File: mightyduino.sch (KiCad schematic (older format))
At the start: 20 parts, among them IC1 ATMEGA644P-A, P1 CONN_01X18, P2 CONN_01X06, P3 CONN_01X18, SW1 RESET, U1 MIC5219-3.3YM5, X1 CSTCE 16MHZ

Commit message: switched led from d13 to d0, cosmetic improvments
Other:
- note added: "<16v"
- note added: "RAW -> input voltage before the voltage regulator \nVCC -> output voltage of the regulator, IC voltage"
- note added: "U1\n MIC5219-xxYM5 -> xx = voltage 1.8->5v\n \nX1\n CSTCE 16MOV53-R0 4-20Mhz"
- note removed: "4-16v"
- note removed: "U1\n MIC5219-3.3YM5 -> 3.3v core\n MIC5219-5.0YM5 -> 5v core\n\nX1\n CSTCE 16MOV53-R0 4-20Mhz"
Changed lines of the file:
@@
 Sheet 1 1
 Title "Mightyduino"
-Date "2016-11-21"
-Rev "1.0"
+Date "2016-12-7"
+Rev "1.1"
 Comp "dev76.org"
 Comment1 "Mightyduino is an arduino based on Atmega 644p/1024p "
@@
 $EndComp
 Text Label 4400 6400 0    59   Italic 0
-D13
+D0
 $Comp
 L CONN_01X06 P2
@@
 RAW
 Text Notes 8900 2000 0    43   ~ 0
-4-16v
+<16v
 $Comp
 L GND #PWR018
@@
 Wire Wire Line
 	2850 7200 2850 7150
-Text Notes 4700 6100 0    60   ~ 0
-U1\n  MIC5219-3.3YM5  -> 3.3v core\n  MIC5219-5.0YM5  -> 5v core\n\nX1\n  CSTCE 16MOV53-R0  4-20Mhz
+Text Notes 8750 6300 0    60   ~ 0
+U1\n  MIC5219-xxYM5  -> xx = voltage 1.8->5v\n  \nX1\n  CSTCE 16MOV53-R0  4-20Mhz
 Wire Wire Line
 	1400 6600 1950 6600
+Text Notes 700  6250 0    60   ~ 0
+RAW -> input voltage before the voltage regulator \nVCC -> output voltage of the regulator, IC voltage
 $EndSCHEMATC

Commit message: updated ressonator 3d design
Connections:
- wire segments 125 -> 126
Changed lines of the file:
@@
 Sheet 1 1
 Title "Mightyduino"
-Date "2016-12-7"
-Rev "1.1"
+Date "2016-12-9"
+Rev "1.2"
 Comp "dev76.org"
 Comment1 "Mightyduino is an arduino based on Atmega 644p/1024p "
@@
 	1    0    0    -1
 $EndComp
-$Comp
-L GND #PWR011
-U 1 1 5841BFB1
-P 1950 6850
-F 0 "#PWR011" H 1950 6600 50  0001 C CNN
-F 1 "GND" H 1950 6700 50  0000 C CNN
-F 2 "" H 1950 6850 50  0000 C CNN
-F 3 "" H 1950 6850 50  0000 C CNN
-	1    1950 6850
-	1    0    0    -1
-$EndComp
 Text Label 900  6600 2    60   ~ 0
 RAW
@@
 $EndComp
 $Comp
-L GND #PWR012
+L GND #PWR011
 U 1 1 5841CAAD
 P 3750 7500
-F 0 "#PWR012" H 3750 7250 50  0001 C CNN
+F 0 "#PWR011" H 3750 7250 50  0001 C CNN
 F 1 "GND" H 3750 7350 50  0000 C CNN
 F 2 "" H 3750 7500 50  0000 C CNN
@@
 $EndComp
 $Comp
-L VCC #PWR013
+L VCC #PWR012
 U 1 1 583847ED
 P 5350 6750
-F 0 "#PWR013" H 5350 6600 50  0001 C CNN
+F 0 "#PWR012" H 5350 6600 50  0001 C CNN
 F 1 "VCC" H 5350 6900 50  0000 C CNN
 F 2 "" H 5350 6750 50  0000 C CNN
@@
 $EndComp
 $Comp
-L GND #PWR014
+L GND #PWR013
 U 1 1 5841EC2B
 P 1400 1200
-F 0 "#PWR014" H 1400 950 50  0001 C CNN
+F 0 "#PWR013" H 1400 950 50  0001 C CNN
 F 1 "GND" H 1400 1050 50  0000 C CNN
 F 2 "" H 1400 1200 50  0000 C CNN
@@
 RAW
 $Comp
-L GND #PWR015
+L GND #PWR014
 U 1 1 584206C2
 P 7750 4700
-F 0 "#PWR015" H 7750 4450 50  0001 C CNN
+F 0 "#PWR014" H 7750 4450 50  0001 C CNN
 F 1 "GND" H 7750 4550 50  0000 C CNN
 F 2 "" H 7750 4700 50  0000 C CNN
@@
 $EndComp
 $Comp
-L GND #PWR016
+L GND #PWR015
 U 1 1 58420BD7
 P 9300 4650
-F 0 "#PWR016" H 9300 4400 50  0001 C CNN
+F 0 "#PWR015" H 9300 4400 50  0001 C CNN
 F 1 "GND" H 9300 4500 50  0000 C CNN
 F 2 "" H 9300 4650 50  0000 C CNN
@@
 $EndComp
 $Comp
-L GND #PWR017
+L GND #PWR016
 U 1 1 5842144D
 P 4850 7350
-F 0 "#PWR017" H 4850 7100 50  0001 C CNN
+F 0 "#PWR016" H 4850 7100 50  0001 C CNN
 F 1 "GND" H 4850 7200 50  0000 C CNN
 F 2 "" H 4850 7350 50  0000 C CNN
@@
 <16v
 $Comp
-L GND #PWR018
+L GND #PWR017
 U 1 1 58422776
 P 9350 1900
-F 0 "#PWR018" H 9350 1650 50  0001 C CNN
+F 0 "#PWR017" H 9350 1650 50  0001 C CNN
 F 1 "GND" H 9350 1750 50  0000 C CNN
 F 2 "" H 9350 1900 50  0000 C CNN
@@
 $EndComp
 $Comp
-L VCC #PWR019
+L VCC #PWR018
 U 1 1 58420A99
 P 7250 4250
-F 0 "#PWR019" H 7250 4100 50  0001 C CNN
+F 0 "#PWR018" H 7250 4100 50  0001 C CNN
 F 1 "VCC" H 7250 4400 50  0000 C CNN
 F 2 "" H 7250 4250 50  0000 C CNN
@@
 $EndComp
 $Comp
-L VCC #PWR020
+L VCC #PWR019
 U 1 1 5841E709
 P 3350 6400
-F 0 "#PWR020" H 3350 6250 50  0001 C CNN
+F 0 "#PWR019" H 3350 6250 50  0001 C CNN
 F 1 "VCC" H 3350 6550 50  0000 C CNN
 F 2 "" H 3350 6400 50  0000 C CNN
@@
 $EndComp
 $Comp
-L VCC #PWR021
+L VCC #PWR020
 U 1 1 58384873
 P 3750 1050
-F 0 "#PWR021" H 3750 900 50  0001 C CNN
+F 0 "#PWR020" H 3750 900 50  0001 C CNN
 F 1 "VCC" H 3750 1200 50  0000 C CNN
 F 2 "" H 3750 1050 50  0000 C CNN
@@
 $EndComp
 $Comp
-L VCC #PWR022
+L VCC #PWR021
 U 1 1 584228A1
 P 8800 1600
-F 0 "#PWR022" H 8800 1450 50  0001 C CNN
+F 0 "#PWR021" H 8800 1450 50  0001 C CNN
 F 1 "VCC" H 8800 1750 50  0000 C CNN
 F 2 "" H 8800 1600 50  0000 C CNN
@@
 Wire Wire Line
 	3750 6600 3750 6800
-Wire Wire Line
-	1950 6850 1950 6750
 Wire Wire Line
 	8700 3650 9100 3650
@@
 	2850 6750 2850 6950
 $Comp
-L GND #PWR023
+L GND #PWR022
 U 1 1 58435E1F
 P 2850 7200
-F 0 "#PWR023" H 2850 6950 50  0001 C CNN
+F 0 "#PWR022" H 2850 6950 50  0001 C CNN
 F 1 "GND" H 2850 7050 50  0000 C CNN
 F 2 "" H 2850 7200 50  0000 C CNN
@@
 Text Notes 700  6250 0    60   ~ 0
 RAW -> input voltage before the voltage regulator \nVCC -> output voltage of the regulator, IC voltage
+Wire Wire Line
+	1950 6750 1900 6750
+Wire Wire Line
+	1900 6750 1900 6600
+Connection ~ 1900 6600
 $EndSCHEMATC

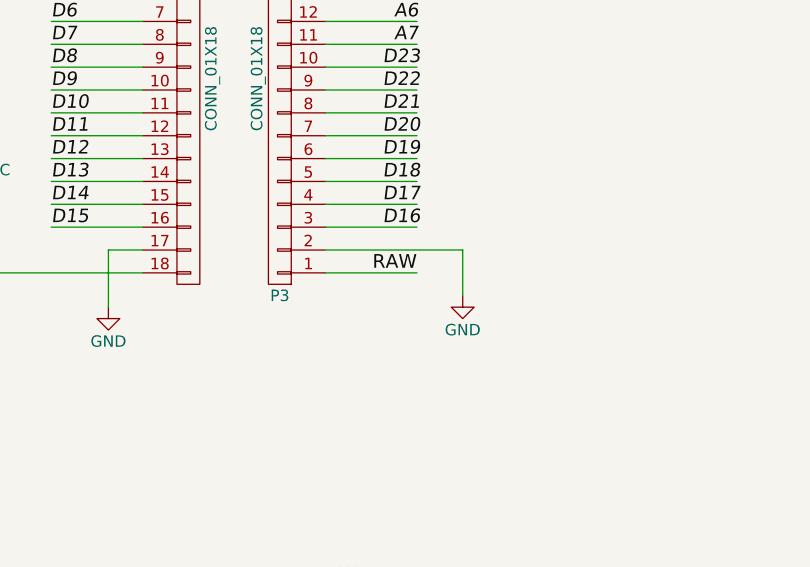
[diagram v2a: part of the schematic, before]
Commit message: C1,C3 better footprint, added RESET PIN
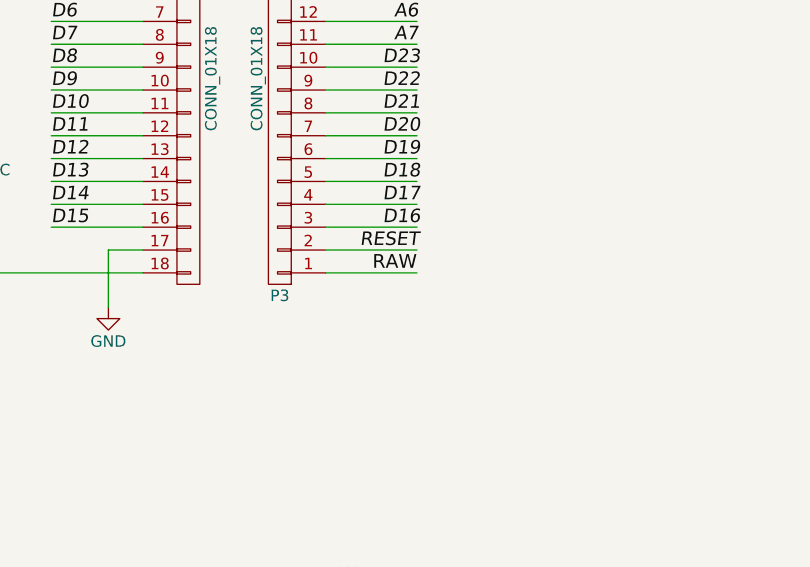
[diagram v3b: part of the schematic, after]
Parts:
- C1, C3: footprint Capacitors_SMD:C_0805 -> Capacitors_Tantalum_SMD:TantalC_SizeA_EIA-3216_Reflow
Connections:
- wire segments 126 -> 125
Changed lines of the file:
@@
 EESchema Schematic File Version 2
+LIBS:mightyduino-rescue
 LIBS:power
 LIBS:device
@@
 Sheet 1 1
 Title "Mightyduino"
-Date "2016-12-9"
-Rev "1.2"
+Date "2017-01-7"
+Rev "1.3"
 Comp "dev76.org"
 Comment1 "Mightyduino is an arduino based on Atmega 644p/1024p "
@@
 $EndComp
 $Comp
-L GND #PWR01
+L GND-RESCUE-mightyduino #PWR01
 U 1 1 58332308
 P 2050 2400
@@
 Murata\nResonator
 $Comp
-L GND #PWR02
+L GND-RESCUE-mightyduino #PWR02
 U 1 1 5833230F
 P 3500 5850
@@
 $EndComp
 $Comp
-L GND #PWR03
+L GND-RESCUE-mightyduino #PWR03
 U 1 1 58332331
 P 2300 3500
@@
 $EndComp
 $Comp
-L GND #PWR04
+L GND-RESCUE-mightyduino #PWR04
 U 1 1 583323B4
 P 5350 7350
@@
 $EndComp
 $Comp
-L GND #PWR06
+L GND-RESCUE-mightyduino #PWR06
 U 1 1 583323CB
 P 5900 7400
@@
 A7
 $Comp
-L GND #PWR07
+L GND-RESCUE-mightyduino #PWR07
 U 1 1 5834C09B
 P 2400 7000
@@
 $EndComp
 $Comp
-L GND #PWR08
+L GND-RESCUE-mightyduino #PWR08
 U 1 1 5834C1DF
 P 3150 7100
@@
 F 0 "C3" H 3360 6920 50  0000 L CNN
 F 1 "10u" H 3360 6770 50  0000 L CNN
-F 2 "Capacitors_SMD:C_0805" H 3350 6850 50  0001 C CNN
+F 2 "Capacitors_Tantalum_SMD:TantalC_SizeA_EIA-3216_Reflow" H 3350 6850 50  0001 C CNN
 F 3 "" H 3350 6850 50  0000 C CNN
 	1    3350 6850
@@
 $EndComp
 $Comp
-L GND #PWR09
+L GND-RESCUE-mightyduino #PWR09
 U 1 1 5838459A
 P 3350 7100
@@
 F 0 "C1" H 1810 6920 50  0000 L CNN
 F 1 "10u" H 1650 6750 50  0000 L CNN
-F 2 "Capacitors_SMD:C_0805" H 1800 6850 50  0001 C CNN
+F 2 "Capacitors_Tantalum_SMD:TantalC_SizeA_EIA-3216_Reflow" H 1800 6850 50  0001 C CNN
 F 3 "" H 1800 6850 50  0000 C CNN
 	1    1800 6850
@@
 $EndComp
 $Comp
-L GND #PWR010
+L GND-RESCUE-mightyduino #PWR010
 U 1 1 58384694
 P 1800 7050
@@
 $EndComp
 $Comp
-L GND #PWR011
+L GND-RESCUE-mightyduino #PWR011
 U 1 1 5841CAAD
 P 3750 7500
@@
 $EndComp
 $Comp
-L GND #PWR013
+L GND-RESCUE-mightyduino #PWR013
 U 1 1 5841EC2B
 P 1400 1200
@@
 RAW
 $Comp
-L GND #PWR014
+L GND-RESCUE-mightyduino #PWR014
 U 1 1 584206C2
 P 7750 4700
@@
 F 3 "" H 7750 4700 50  0000 C CNN
 	1    7750 4700
-	1    0    0    -1
-$EndComp
-$Comp
-L GND #PWR015
-U 1 1 58420BD7
-P 9300 4650
-F 0 "#PWR015" H 9300 4400 50  0001 C CNN
-F 1 "GND" H 9300 4500 50  0000 C CNN
-F 2 "" H 9300 4650 50  0000 C CNN
-F 3 "" H 9300 4650 50  0000 C CNN
-	1    9300 4650
 	1    0    0    -1
 $EndComp
@@
 $EndComp
 $Comp
-L GND #PWR016
+L GND-RESCUE-mightyduino #PWR015
 U 1 1 5842144D
 P 4850 7350
-F 0 "#PWR016" H 4850 7100 50  0001 C CNN
+F 0 "#PWR015" H 4850 7100 50  0001 C CNN
 F 1 "GND" H 4850 7200 50  0000 C CNN
 F 2 "" H 4850 7350 50  0000 C CNN
@@
 <16v
 $Comp
-L GND #PWR017
+L GND-RESCUE-mightyduino #PWR016
 U 1 1 58422776
 P 9350 1900
-F 0 "#PWR017" H 9350 1650 50  0001 C CNN
+F 0 "#PWR016" H 9350 1650 50  0001 C CNN
 F 1 "GND" H 9350 1750 50  0000 C CNN
 F 2 "" H 9350 1900 50  0000 C CNN
@@
 $EndComp
 $Comp
-L VCC #PWR018
+L VCC #PWR017
 U 1 1 58420A99
 P 7250 4250
-F 0 "#PWR018" H 7250 4100 50  0001 C CNN
+F 0 "#PWR017" H 7250 4100 50  0001 C CNN
 F 1 "VCC" H 7250 4400 50  0000 C CNN
 F 2 "" H 7250 4250 50  0000 C CNN
@@
 $EndComp
 $Comp
-L VCC #PWR019
+L VCC #PWR018
 U 1 1 5841E709
 P 3350 6400
-F 0 "#PWR019" H 3350 6250 50  0001 C CNN
+F 0 "#PWR018" H 3350 6250 50  0001 C CNN
 F 1 "VCC" H 3350 6550 50  0000 C CNN
 F 2 "" H 3350 6400 50  0000 C CNN
@@
 $EndComp
 $Comp
-L VCC #PWR020
+L VCC #PWR019
 U 1 1 58384873
 P 3750 1050
-F 0 "#PWR020" H 3750 900 50  0001 C CNN
+F 0 "#PWR019" H 3750 900 50  0001 C CNN
 F 1 "VCC" H 3750 1200 50  0000 C CNN
 F 2 "" H 3750 1050 50  0000 C CNN
@@
 $EndComp
 $Comp
-L VCC #PWR021
+L VCC #PWR020
 U 1 1 584228A1
 P 8800 1600
-F 0 "#PWR021" H 8800 1450 50  0001 C CNN
+F 0 "#PWR020" H 8800 1450 50  0001 C CNN
 F 1 "VCC" H 8800 1750 50  0000 C CNN
 F 2 "" H 8800 1600 50  0000 C CNN
@@
 	4850 7000 4850 6850
 Wire Wire Line
-	9300 4450 9300 4650
-Wire Wire Line
 	7250 4550 7900 4550
 Wire Wire Line
@@
 	7750 4450 7750 4700
 Wire Wire Line
-	8700 4450 9300 4450
+	8700 4450 9100 4450
 Wire Wire Line
 	7750 4450 7900 4450
@@
 	2850 6750 2850 6950
 $Comp
-L GND #PWR022
+L GND-RESCUE-mightyduino #PWR021
 U 1 1 58435E1F
 P 2850 7200
-F 0 "#PWR022" H 2850 6950 50  0001 C CNN
+F 0 "#PWR021" H 2850 6950 50  0001 C CNN
 F 1 "GND" H 2850 7050 50  0000 C CNN
 F 2 "" H 2850 7200 50  0000 C CNN
@@
 	1900 6750 1900 6600
 Connection ~ 1900 6600
+Text Label 8850 4450 0    59   Italic 0
+RESET
 $EndSCHEMATC
